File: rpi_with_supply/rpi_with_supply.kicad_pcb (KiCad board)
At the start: 2 copper layers, 65 x 56 mm, 34 parts, among them J3 Phoenix 1933189 COMBICON, J4 Phoenix 1933189 COMBICON, J5 Raspberry_Pi_2_3, P1 CONN_1, P10 CONN_02X02, P2 CONN_1, P3 CONN_1, P4 CONN_1, P5 CONN_1, P6 CONN_1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

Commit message: bump to rev A
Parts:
- added J6: FAN, Socket_Strip_Straight_1x02_Pitch2.54mm, F.Cu at (37.2, 27.0)
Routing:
- net GND: track 386.7 -> 403.4 mm, vias 5 -> 6
- net PI_PWR: track 99.5 -> 104.1 mm
- net HT: track 303.1 -> 301.0 mm
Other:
- board text added: "+"
- board text added: "-"
- board text added: "cnpihats rpi_with_supply revA (C) <>< 2018 C. Lohr"
- board text removed: "cnpihats rpi_with_supply rev- (C) <>< 2018 C. Lohr"

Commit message: bump to rev b
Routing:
- net (no net): track 0.00 -> 1.57 mm
- net GND: track 403.4 -> 401.9 mm
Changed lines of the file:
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@@
-(kicad_pcb (version 4) (host pcbnew 4.0.7-e2-6376~58~ubuntu16.04.1)
+(kicad_pcb (version 4) (host pcbnew 4.0.2+dfsg1-stable)
   (general
     (links 93)
     (no_connects 0)
-    (area 14.224 12.6718 87.884001 74.0782)
+    (area 14.224 12.5218 87.884001 73.9782)
     (thickness 1.6)
-    (drawings 25)
+    (drawings 40)
     (tracks 345)
     (zones 0)
@@
       (drillshape 0)
       (scaleselection 1)
-      (outputdirectory rpi_with_supply_revA))
+      (outputdirectory rpi_with_supply_revB))
   )
   (net 0 "")
@@
       (effects (font (size 1 1) (thickness 0.15)))
     )
-    (fp_text value 10k (at 0 1.75 180) (layer F.Fab)
+    (fp_text value 10k (at 0.164 -2.089 180) (layer F.SilkS)
       (effects (font (size 1 1) (thickness 0.15)))
     )
@@
     )
   )
+  (gr_line (start 55.245 61.595) (end 55.245 64.135) (angle 90) (layer F.SilkS) (width 0.2))
+  (gr_line (start 53.975 62.865) (end 56.515 62.865) (angle 90) (layer F.SilkS) (width 0.2))
+  (gr_line (start 48.26 62.865) (end 50.8 62.865) (angle 90) (layer F.SilkS) (width 0.2))
+  (gr_line (start 25.4 69.85) (end 25.4 67.945) (angle 90) (layer F.SilkS) (width 0.2))
+  (gr_line (start 39.37 69.215) (end 39.37 66.675) (angle 90) (layer F.SilkS) (width 0.2))
+  (gr_line (start 38.1 67.945) (end 40.64 67.945) (angle 90) (layer F.SilkS) (width 0.2))
+  (gr_line (start 41.91 65.405) (end 41.91 64.135) (angle 90) (layer F.SilkS) (width 0.2))
+  (gr_line (start 44.45 64.77) (end 45.72 64.77) (angle 90) (layer F.SilkS) (width 0.2))
+  (gr_line (start 45.085 65.405) (end 45.085 64.135) (angle 90) (layer F.SilkS) (width 0.2))
+  (gr_line (start 50.8 29.21) (end 50.8 30.48) (angle 90) (layer F.SilkS) (width 0.2))
+  (gr_line (start 46.99 29.845) (end 48.26 29.845) (angle 90) (layer F.SilkS) (width 0.2))
+  (gr_line (start 47.625 29.21) (end 47.625 30.48) (angle 90) (layer F.SilkS) (width 0.2))
+  (gr_line (start 29.845 29.21) (end 31.115 29.21) (angle 90) (layer F.SilkS) (width 0.2))
+  (gr_line (start 30.48 26.035) (end 30.48 24.765) (angle 90) (layer F.SilkS) (width 0.2))
+  (gr_line (start 29.845 25.4) (end 31.115 25.4) (angle 90) (layer F.SilkS) (width 0.2))
   (gr_text - (at 40.03 26.49) (layer F.SilkS)
     (effects (font (size 1.5 1.5) (thickness 0.3)))
@@
   (gr_line (start 68.04 52.832) (end 68.04 53.848) (angle 90) (layer F.SilkS) (width 0.2))
   (gr_line (start 68.548 53.34) (end 68.04 52.832) (angle 90) (layer F.SilkS) (width 0.2))
+  (segment (start 31.25 20.19) (end 31.25 21.73) (width 0.3302) (layer F.Cu) (net 0))
+  (segment (start 31.25 21.73) (end 31.27 21.75) (width 0.3302) (layer F.Cu) (net 0))
   (segment (start 34.52395 27.52395) (end 33.4 26.4) (width 0.3302) (layer F.Cu) (net 1))
   (segment (start 33.4 26.4) (end 32 26.4) (width 0.3302) (layer F.Cu) (net 1))
@@
   (segment (start 26.55 33.95) (end 25 35.5) (width 0.6) (layer F.Cu) (net 1))
   (segment (start 25 35.5) (end 25 36.19) (width 0.6) (layer F.Cu) (net 1))
-  (segment (start 31.25 20.19) (end 31.25 21.73) (width 0.3302) (layer F.Cu) (net 2))
-  (segment (start 31.25 21.73) (end 31.27 21.75) (width 0.3302) (layer F.Cu) (net 2))
   (segment (start 31.24 20.15) (end 31.71 20.15) (width 0.3302) (layer B.Cu) (net 2))
   (segment (start 33.77 20.22) (end 33.77 21.67) (width 0.3302) (layer B.Cu) (net 2))
@@
   (segment (start 31.86 20) (end 33.55 20) (width 0.3302) (layer B.Cu) (net 2))
   (segment (start 31.71 20.15) (end 31.86 20) (width 0.3302) (layer B.Cu) (net 2))
-  (segment (start 29.95 18.73) (end 30.07 18.73) (width 0.3302) (layer B.Cu) (net 2) (status C00000))
-  (segment (start 30.07 18.73) (end 31.24 19.9) (width 0.3302) (layer B.Cu) (net 2) (status 400000))
+  (segment (start 29.95 18.73) (end 30.07 18.73) (width 0.3302) (layer B.Cu) (net 2))
+  (segment (start 30.07 18.73) (end 31.24 19.9) (width 0.3302) (layer B.Cu) (net 2))
   (segment (start 31.24 19.9) (end 31.24 20.15) (width 0.3302) (layer B.Cu) (net 2))
   (segment (start 31.24 20.15) (end 31.24 22.24) (width 0.3302) (layer B.Cu) (net 2))
-  (segment (start 37.17 26.97) (end 37.14 26.97) (width 0.3302) (layer B.Cu) (net 2) (status C00000))
-  (segment (start 37.14 26.97) (end 36.28 27.83) (width 0.3302) (layer B.Cu) (net 2) (status 400000))
-  (segment (start 37.14 26.97) (end 36.28 27.83) (width 0.3302) (layer F.Cu) (net 2) (status 400000))
-  (segment (start 37.17 26.97) (end 36.53 26.97) (width 0.3302) (layer F.Cu) (net 2) (status C00000))
-  (segment (start 36.53 26.97) (end 34.95 25.39) (width 0.3302) (layer F.Cu) (net 2) (status 400000))
+  (segment (start 37.17 26.97) (end 37.14 26.97) (width 0.3302) (layer B.Cu) (net 2))
+  (segment (start 37.14 26.97) (end 36.28 27.83) (width 0.3302) (layer B.Cu) (net 2))
+  (segment (start 37.14 26.97) (end 36.28 27.83) (width 0.3302) (layer F.Cu) (net 2))
+  (segment (start 37.17 26.97) (end 36.53 26.97) (width 0.3302) (layer F.Cu) (net 2))
+  (segment (start 36.53 26.97) (end 34.95 25.39) (width 0.3302) (layer F.Cu) (net 2))
   (segment (start 34.71 31.27539) (end 32.82539 33.16) (width 0.3302) (layer F.Cu) (net 2))
   (segment (start 37.97 28.01539) (end 34.71 31.27539) (width 0.3302) (layer F.Cu) (net 2))

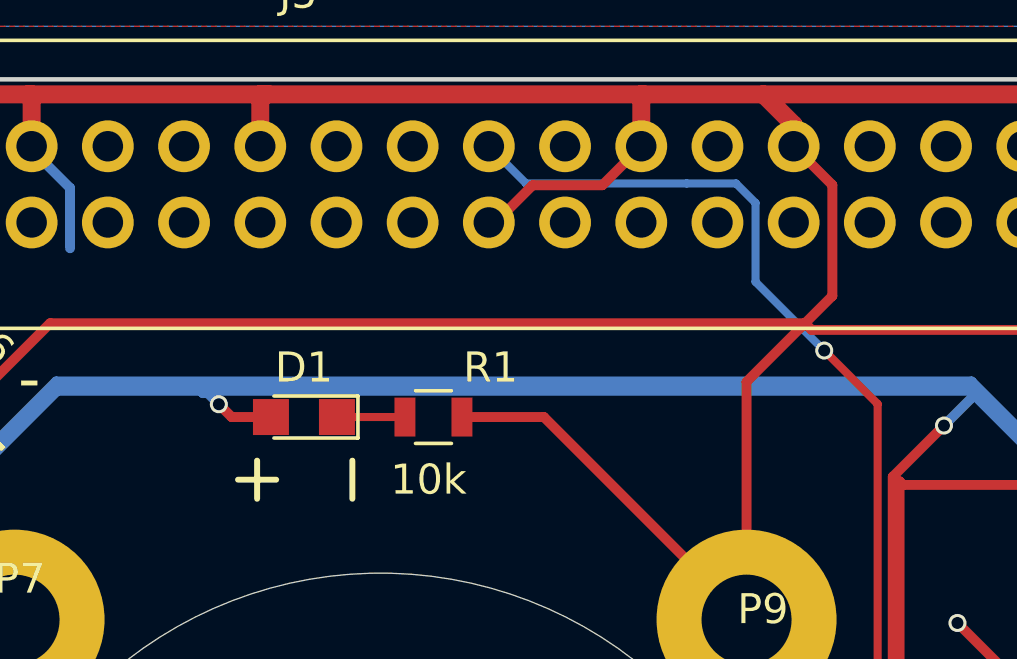
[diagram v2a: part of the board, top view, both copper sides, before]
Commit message: Bump design with pull up
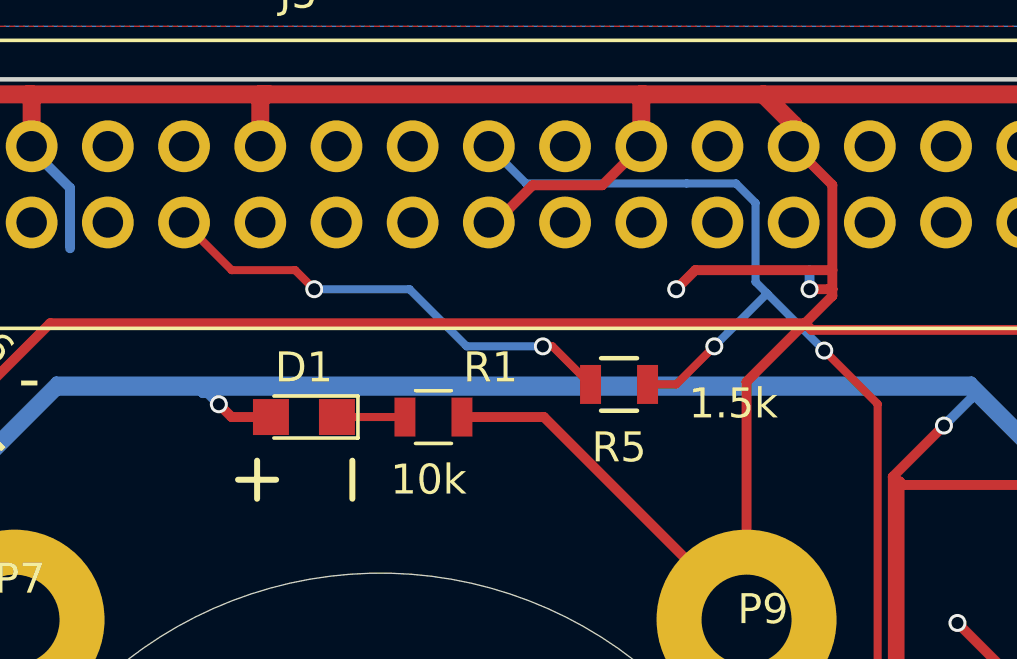
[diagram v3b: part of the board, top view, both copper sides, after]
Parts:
- added R5: 1.5k, R_0805, F.Cu at (59.7, 26.7)
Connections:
- J5 pad 17: (no net) -> Net-(J5-Pad17)
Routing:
- net Net-(J5-Pad17): track 0.00 -> 15.8 mm, vias 0 -> 2
- net GND: track 401.9 -> 409.0 mm, vias 6 -> 8
- net INPUT: track 66.9 -> 72.1 mm, vias 3 -> 4
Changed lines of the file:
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@@
 (kicad_pcb (version 4) (host pcbnew 4.0.2+dfsg1-stable)
   (general
-    (links 93)
+    (links 95)
     (no_connects 0)
-    (area 14.224 12.5218 87.884001 73.9782)
+    (area 16.424999 16.424999 81.575001 72.575001)
     (thickness 1.6)
     (drawings 40)
-    (tracks 345)
+    (tracks 370)
     (zones 0)
-    (modules 35)
-    (nets 14)
+    (modules 36)
+    (nets 15)
   )
   (page User 200 200)
@@
   (net 12 OUT)
   (net 13 INPUT)
+  (net 14 "Net-(J5-Pad17)")
   (net_class Default "This is the default net class."
     (clearance 0.2032)
@@
     (add_net "Net-(D2-Pad1)")
     (add_net "Net-(D3-Pad1)")
+    (add_net "Net-(J5-Pad17)")
     (add_net "Net-(R4-Pad1)")
     (add_net "Net-(R6-Pad1)")
@@
     (pad 15 thru_hole oval (at 17.78 0) (size 1.7272 1.7272) (drill 1.016) (layers *.Cu *.Mask))
     (pad 16 thru_hole oval (at 17.78 -2.54) (size 1.7272 1.7272) (drill 1.016) (layers *.Cu *.Mask))
-    (pad 17 thru_hole oval (at 20.32 0) (size 1.7272 1.7272) (drill 1.016) (layers *.Cu *.Mask))
+    (pad 17 thru_hole oval (at 20.32 0) (size 1.7272 1.7272) (drill 1.016) (layers *.Cu *.Mask)
+      (net 14 "Net-(J5-Pad17)"))
     (pad 18 thru_hole oval (at 20.32 -2.54) (size 1.7272 1.7272) (drill 1.016) (layers *.Cu *.Mask))
     (pad 19 thru_hole oval (at 22.86 0) (size 1.7272 1.7272) (drill 1.016) (layers *.Cu *.Mask))
@@
       (scale (xyz 1 1 1))
       (rotate (xyz 0 0 270))
+    )
+  )
+  (module R_0805 (layer F.Cu)
+    (at 59.69 26.67 180)
+    (descr "Resistor SMD 0805, reflow soldering, Vishay (see dcrcw.pdf)")
+    (tags "resistor 0805")
+    (attr smd)
+    (fp_text reference R5 (at 0 -2.1 180) (layer F.SilkS)
+      (effects (font (size 1 1) (thickness 0.15)))
+    )
+    (fp_text value 1.5k (at -3.81 -0.635 180) (layer F.SilkS)
+      (effects (font (size 1 1) (thickness 0.15)))
+    )
+    (fp_line (start -1.6 -1) (end 1.6 -1) (layer F.CrtYd) (width 0.05))
+    (fp_line (start -1.6 1) (end 1.6 1) (layer F.CrtYd) (width 0.05))
+    (fp_line (start -1.6 -1) (end -1.6 1) (layer F.CrtYd) (width 0.05))
+    (fp_line (start 1.6 -1) (end 1.6 1) (layer F.CrtYd) (width 0.05))
+    (fp_line (start 0.6 0.875) (end -0.6 0.875) (layer F.SilkS) (width 0.15))
+    (fp_line (start -0.6 -0.875) (end 0.6 -0.875) (layer F.SilkS) (width 0.15))
+    (pad 1 smd rect (at -0.95 0 180) (size 0.7 1.3) (layers F.Cu F.Paste F.Mask)
+      (net 13 INPUT))
+    (pad 2 smd rect (at 0.95 0 180) (size 0.7 1.3) (layers F.Cu F.Paste F.Mask)
+      (net 14 "Net-(J5-Pad17)"))
+    (model Resistors_SMD.3dshapes/R_0805.wrl
+      (at (xyz 0 0 0))
+      (scale (xyz 1 1 1))
+      (rotate (xyz 0 0 0))
     )
   )
@@
   (segment (start 26.55 33.95) (end 25 35.5) (width 0.6) (layer F.Cu) (net 1))
   (segment (start 25 35.5) (end 25 36.19) (width 0.6) (layer F.Cu) (net 1))
+  (segment (start 66.04 22.86) (end 66.04 23.495) (width 0.3302) (layer B.Cu) (net 2))
+  (segment (start 66.04 23.495) (end 66.8 23.495) (width 0.3302) (layer F.Cu) (net 2))
+  (via (at 66.04 23.495) (size 0.6) (drill 0.4) (layers F.Cu B.Cu) (net 2))
+  (segment (start 66.8 23.495) (end 66.675 23.495) (width 0.3302) (layer F.Cu) (net 2))
+  (segment (start 66.675 23.495) (end 66.8 23.495) (width 0.3302) (layer F.Cu) (net 2))
+  (segment (start 66.8 22.86) (end 62.23 22.86) (width 0.3302) (layer F.Cu) (net 2))
+  (via (at 61.595 23.495) (size 0.6) (drill 0.4) (layers F.Cu B.Cu) (net 2))
+  (segment (start 62.23 22.86) (end 61.595 23.495) (width 0.3302) (layer F.Cu) (net 2))
   (segment (start 31.24 20.15) (end 31.71 20.15) (width 0.3302) (layer B.Cu) (net 2))
   (segment (start 33.77 20.22) (end 33.77 21.67) (width 0.3302) (layer B.Cu) (net 2))
@@
   (segment (start 63.94 26.58) (end 65.89 24.63) (width 0.3302) (layer F.Cu) (net 2))
   (segment (start 65.89 24.63) (end 66.8 23.72) (width 0.3302) (layer F.Cu) (net 2))
-  (segment (start 66.8 23.72) (end 66.8 20.02) (width 0.3302) (layer F.Cu) (net 2))
+  (segment (start 66.8 23.72) (end 66.8 23.495) (width 0.3302) (layer F.Cu) (net 2))
+  (segment (start 66.8 23.495) (end 66.8 22.86) (width 0.3302) (layer F.Cu) (net 2))
+  (segment (start 66.8 22.86) (end 66.8 20.02) (width 0.3302) (layer F.Cu) (net 2))
   (segment (start 66.8 20.02) (end 65.51 18.73) (width 0.3302) (layer F.Cu) (net 2))
   (segment (start 32.47 33.16) (end 32.47 51.988) (width 0.3302) (layer F.Cu) (net 2))
@@
   (segment (start 47.35 64.5) (end 52.41 64.5) (width 0.27) (layer F.Cu) (net 12))
   (segment (start 52.41 64.5) (end 55.88 67.97) (width 0.27) (layer F.Cu) (net 12))
+  (segment (start 64.6275 23.6375) (end 62.865 25.4) (width 0.27) (layer B.Cu) (net 13))
+  (segment (start 61.595 26.67) (end 60.64 26.67) (width 0.27) (layer F.Cu) (net 13) (status 800000))
+  (segment (start 62.865 25.4) (end 61.595 26.67) (width 0.27) (layer F.Cu) (net 13))
+  (via (at 62.865 25.4) (size 0.6) (drill 0.4) (layers F.Cu B.Cu) (net 13))
   (segment (start 61.95 19.97) (end 56.59 19.97) (width 0.27) (layer B.Cu) (net 13))
   (segment (start 56.59 19.97) (end 55.35 18.73) (width 0.27) (layer B.Cu) (net 13))
@@
   (segment (start 68.31 27.32) (end 66.53 25.54) (width 0.27) (layer F.Cu) (net 13))
   (via (at 66.53 25.54) (size 0.6) (drill 0.4) (layers F.Cu B.Cu) (net 13))
-  (segment (start 66.53 25.54) (end 64.24 23.25) (width 0.27) (layer B.Cu) (net 13))
+  (segment (start 66.53 25.54) (end 64.6275 23.6375) (width 0.27) (layer B.Cu) (net 13))
+  (segment (start 64.6275 23.6375) (end 64.24 23.25) (width 0.27) (layer B.Cu) (net 13))
   (segment (start 64.24 23.25) (end 64.24 20.62) (width 0.27) (layer B.Cu) (net 13))
   (segment (start 64.24 20.62) (end 63.59 19.97) (width 0.27) (layer B.Cu) (net 13))
   (segment (start 63.59 19.97) (end 61.95 19.97) (width 0.27) (layer B.Cu) (net 13))
+  (segment (start 58.74 26.67) (end 57.47 25.4) (width 0.27) (layer F.Cu) (net 14) (status 400000))
+  (segment (start 46.78 22.86) (end 45.19 21.27) (width 0.27) (layer F.Cu) (net 14) (status 800000))
+  (segment (start 48.895 22.86) (end 46.78 22.86) (width 0.27) (layer F.Cu) (net 14))
+  (segment (start 49.53 23.495) (end 48.895 22.86) (width 0.27) (layer F.Cu) (net 14))
+  (via (at 49.53 23.495) (size 0.6) (drill 0.4) (layers F.Cu B.Cu) (net 14))
+  (segment (start 52.705 23.495) (end 49.53 23.495) (width 0.27) (layer B.Cu) (net 14))
+  (segment (start 54.61 25.4) (end 52.705 23.495) (width 0.27) (layer B.Cu) (net 14))
+  (segment (start 57.15 25.4) (end 54.61 25.4) (width 0.27) (layer B.Cu) (net 14))
+  (via (at 57.15 25.4) (size 0.6) (drill 0.4) (layers F.Cu B.Cu) (net 14))
+  (segment (start 57.47 25.4) (end 57.15 25.4) (width 0.27) (layer F.Cu) (net 14))
   (zone (net 2) (net_name GND) (layer B.Cu) (hatch edge 0.508)
     (connect_pads (clearance 0.3))

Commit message: update design
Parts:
- added C8: .1u, C_0805, F.Cu at (45.1, 26.9)
- added D5: RED, LED_0805, F.Cu at (34.8, 26.1)
- added IC1: ATTINY85-S, SOIC-8-WIDE, F.Cu at (52.5, 26.1)
- added P11: WS2812, Pin_Header_Straight_1x03, F.Cu at (43.4, 24.2)
- added Q1: Q_NMOS_GDS, SOT-23, F.Cu at (41.2, 27.3)
- added R7: 10k, R_0805, F.Cu at (58.9, 24.5)
- added R9: 1.5k, R_0805, F.Cu at (58.9, 26.7)
- moved R1 44.7 mm to (41.3, 70.8)
- moved D1 40.3 mm to (41.8, 67.4), turned to 90 degrees
- moved R5 7.24 mm to (66.7, 28.5)
- moved R2 2.04 mm to (45.2, 70.8), turned to 0 degrees
- moved D2 1.66 mm to (45.3, 67.5), turned to 90 degrees
- moved J3 1.51 mm to (33.4, 68.0)
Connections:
- net Net-(J5-Pad17) renamed +3V3
- J5 pad 19: (no net) -> MOSI
- J5 pad 21: (no net) -> MISO
- J5 pad 23: (no net) -> SCK
- J5 pad 24: (no net) -> ~AVRRST~
- J6 pad 1: GND -> Net-(D5-Pad2)
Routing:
- net GND: track 409.0 -> 381.9 mm, vias 8 -> 14
- net Net-(IC1-Pad3): track 0.00 -> 24.5 mm, vias 0 -> 1
- net FANCTL: track 0.00 -> 20.5 mm, vias 0 -> 2
- net HT: track 301.0 -> 315.8 mm
- net +3V3: track 15.8 -> 28.1 mm
- net ~AVRRST~: track 0.00 -> 11.6 mm
- net PI_PWR: track 104.1 -> 113.4 mm
- net SCK: track 0.00 -> 7.50 mm
- net Net-(D5-Pad2): track 0.00 -> 6.71 mm
- net MISO: track 0.00 -> 5.22 mm
- net INPUT: track 72.1 -> 67.7 mm, vias 4 -> 3
- net MOSI: track 0.00 -> 3.62 mm
- net Net-(D1-Pad1): track 2.27 -> 3.38 mm
- net OUT: track 28.6 -> 27.7 mm
- net (no net): track 1.57 -> 2.15 mm
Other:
- board text added: "cnpihats rpi_with_supply rev B (C) <>< 2018 C. Lohr"
- board text removed: "cnpihats rpi_with_supply revA (C) <>< 2018 C. Lohr"

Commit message: bump
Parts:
- IC1: value ATTINY85-S -> ATTINY25
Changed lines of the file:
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@@
   (module PHOENIX1933189 (layer F.Cu)
     (at 33.4 68)
-    (fp_text reference J3 (at -6.546 -2.922) (layer F.SilkS)
+    (fp_text reference J3 (at 1.525 -3.865 90) (layer F.SilkS)
       (effects (font (size 1 1) (thickness 0.15)))
     )
@@
     (tags "resistor 0805")
     (attr smd)
-    (fp_text reference R4 (at 2.032 0.127 90) (layer F.SilkS)
-      (effects (font (size 1 1) (thickness 0.15)))
-    )
-    (fp_text value 63.4k (at 1.397 -2.54 90) (layer F.SilkS)
+    (fp_text reference R4 (at 1.17 2.08 270) (layer F.SilkS)
+      (effects (font (size 1 1) (thickness 0.15)))
+    )
+    (fp_text value 63.4k (at -1.37 3.35 90) (layer F.SilkS)
       (effects (font (size 1 1) (thickness 0.15)))
     )
@@
       (effects (font (size 1 1) (thickness 0.15)))
     )
-    (fp_text value A8498 (at 0.381 0.127 180) (layer F.Fab)
+    (fp_text value A8498 (at -1.428 7.554 180) (layer F.SilkS)
       (effects (font (size 1 1) (thickness 0.15)))
     )
@@
       (effects (font (size 1 1) (thickness 0.15)))
     )
-    (fp_text value .1u (at 0 2.1 180) (layer F.SilkS)
+    (fp_text value .1u (at 0.015 -3.58 180) (layer F.SilkS)
       (effects (font (size 1 1) (thickness 0.15)))
     )
@@
     (tags "CMS SOJ")
     (attr smd)
-    (fp_text reference IC1 (at 0 -1.27 90) (layer F.SilkS)
-      (effects (font (size 1 1) (thickness 0.15)))
-    )
-    (fp_text value ATTINY85-S (at -4.3 -0.3 180) (layer F.SilkS)
+    (fp_text reference IC1 (at -4.38 4.015 90) (layer F.SilkS)
+      (effects (font (size 1 1) (thickness 0.15)))
+    )
+    (fp_text value ATTINY25 (at -4.3 -0.3 180) (layer F.SilkS)
       (effects (font (size 1 1) (thickness 0.15)))
     )
@@
       (effects (font (size 1 1) (thickness 0.15)))
     )
-    (fp_text value Q_NMOS_GDS (at 0 2.3 180) (layer F.Fab)
+    (fp_text value Q_NMOS_GDS (at -1.98 -3.815 180) (layer F.Fab)
       (effects (font (size 1 1) (thickness 0.15)))
     )
@@
     (descr "Through hole pin header")
     (tags "pin header")
-    (fp_text reference P11 (at 0 -5.1 270) (layer F.SilkS)
+    (fp_text reference P11 (at -0.705 7.84 360) (layer F.SilkS)
       (effects (font (size 1 1) (thickness 0.15)))
     )
@@
   (gr_line (start 53.975 62.865) (end 56.515 62.865) (angle 90) (layer F.SilkS) (width 0.2))
   (gr_line (start 48.26 62.865) (end 50.8 62.865) (angle 90) (layer F.SilkS) (width 0.2))
-  (gr_line (start 25.4 69.85) (end 25.4 67.945) (angle 90) (layer F.SilkS) (width 0.2))
+  (gr_line (start 26.67 71.755) (end 26.67 69.85) (angle 90) (layer F.SilkS) (width 0.2))
   (gr_line (start 39.37 69.215) (end 39.37 66.675) (angle 90) (layer F.SilkS) (width 0.2))
   (gr_line (start 38.1 67.945) (end 40.64 67.945) (angle 90) (layer F.SilkS) (width 0.2))

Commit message: bump
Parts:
- added SW1: PWR, TACTILE10, F.Cu at (75.0, 32.5)
- Q1: value Q_NMOS_GDS -> 2N7002
- moved Q1 0.85 mm to (41.3, 28.1), turned to 45 degrees
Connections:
- J5 pad 40: (no net) -> GPIO21
- Q1 pad 2: Net-(D5-Pad2) -> GND
- Q1 pad 3: GND -> Net-(D5-Pad2)
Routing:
- net GND: track 381.9 -> 418.7 mm, vias 14 -> 16
- net GPIO21: track 0.00 -> 15.0 mm, vias 0 -> 1
- net HT: track 315.8 -> 308.3 mm, vias 4 -> 5
- net (no net): track 2.15 -> 0.00 mm
- net FANCTL: track 20.5 -> 19.5 mm
- net INPUT: track 67.7 -> 68.3 mm
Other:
- board text added: "cnpihats rpi_with_supply rev C (C) <>< 2018 C. Lohr"
- board text removed: "cnpihats rpi_with_supply rev B (C) <>< 2018 C. Lohr"

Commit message: bump design
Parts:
- removed D3: GRN, LED_0805
- removed R5: 1.5k, R_0805
- added D6: BLU, LED_0805, F.Cu at (40.6, 27.4)
- added P12: UPDI, Pin_Header_Straight_1x03, F.Cu at (36.4, 26.4)
- added Q2: FDV304P, SOT-23, F.Cu at (43.4, 24.2)
- added Q3: DMN2046, SOT-23, F.Cu at (46.0, 28.1)
- added R10: 1k, R_0805, F.Cu at (37.4, 23.7)
- added R11: 10k, R_0805, F.Cu at (33.6, 23.6)
- Q1: value 2N7002 -> DMN2046
- R3: value 1k -> 10k
- moved P11 22.7 mm to (33.4, 44.5), turned to 180 degrees
- moved R3 17.0 mm to (46.2, 24.4), turned to 270 degrees
- moved C8 7.97 mm to (52.6, 29.6)
- moved J6 7.74 mm to (33.7, 33.9), turned to 0 degrees
- moved Q1 6.29 mm to (35.3, 29.7), turned to 90 degrees
- moved D5 5.71 mm to (31.1, 30.5), turned to 0 degrees
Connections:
- J5 pad 10: (no net) -> TXRX
- J5 pad 11: (no net) -> GPIO17
- J5 pad 8: (no net) -> Net-(J5-Pad8)
- R3 pad 2: GND -> HT
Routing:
- net GND: track 418.7 -> 482.2 mm, vias 16 -> 14
- net Net-(IC1-Pad3): track 24.5 -> 44.9 mm, vias 1 -> 2
- net GPIO17: track 0.00 -> 11.7 mm
- net Net-(P12-Pad2): track 0.00 -> 11.3 mm
- net PI_PWR: track 113.4 -> 122.9 mm
- net TXRX: track 0.00 -> 9.34 mm
- net Net-(J5-Pad8): track 0.00 -> 6.16 mm
- net FANCTL: track 19.5 -> 25.1 mm
- net Net-(Q2-Pad1): track 2.63 -> 7.22 mm
- net HT: track 308.3 -> 311.7 mm, vias 5 -> 7
- net +3V3: track 28.1 -> 29.4 mm, vias 2 -> 0
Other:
- board text added: "WS"
- board text added: "cnpihats rpi_with_supply rev D (C) <>< 2018 C. Lohr"
- board text removed: "cnpihats rpi_with_supply rev C (C) <>< 2018 C. Lohr"
